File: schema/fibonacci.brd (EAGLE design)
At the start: 88.9 x 59.7 mm, 29 parts, among them IC1 ATMEGA328P, IC2 DS1307

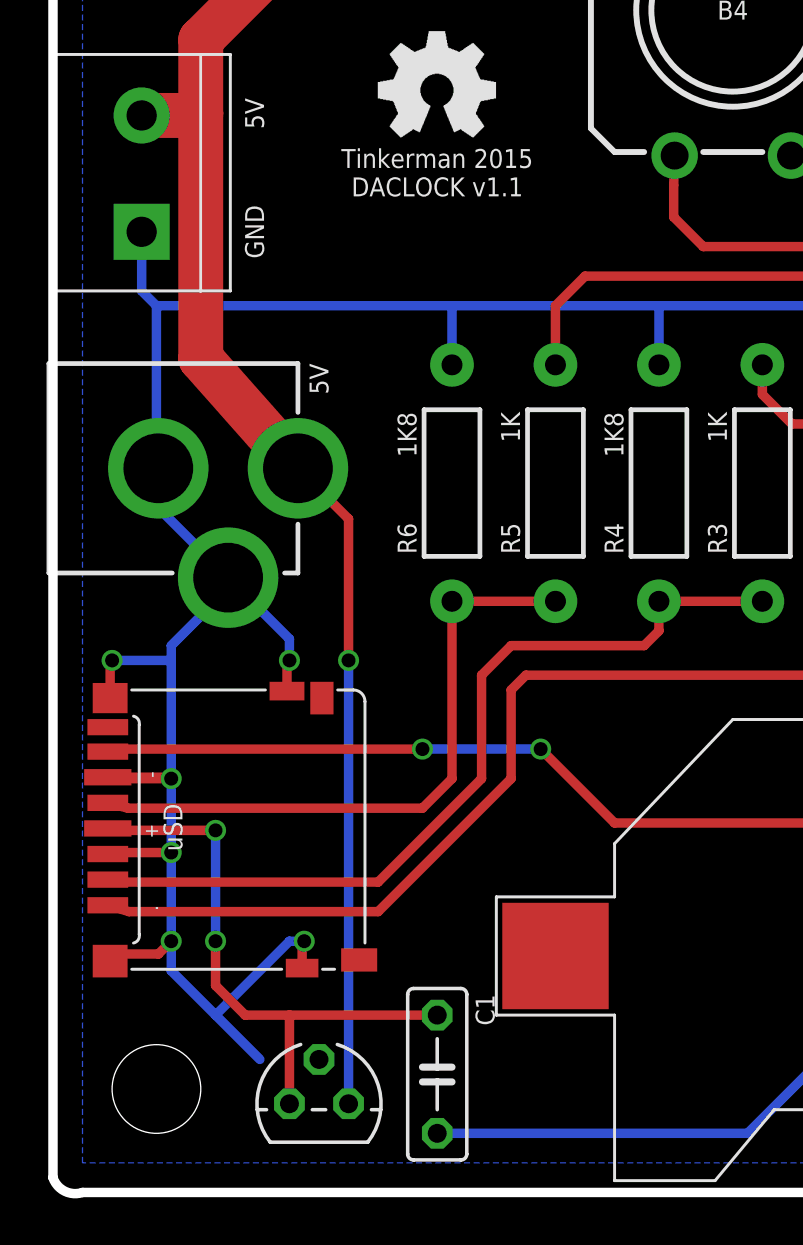
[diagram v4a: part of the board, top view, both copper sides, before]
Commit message: Version 1.2 of the layout sent to fab
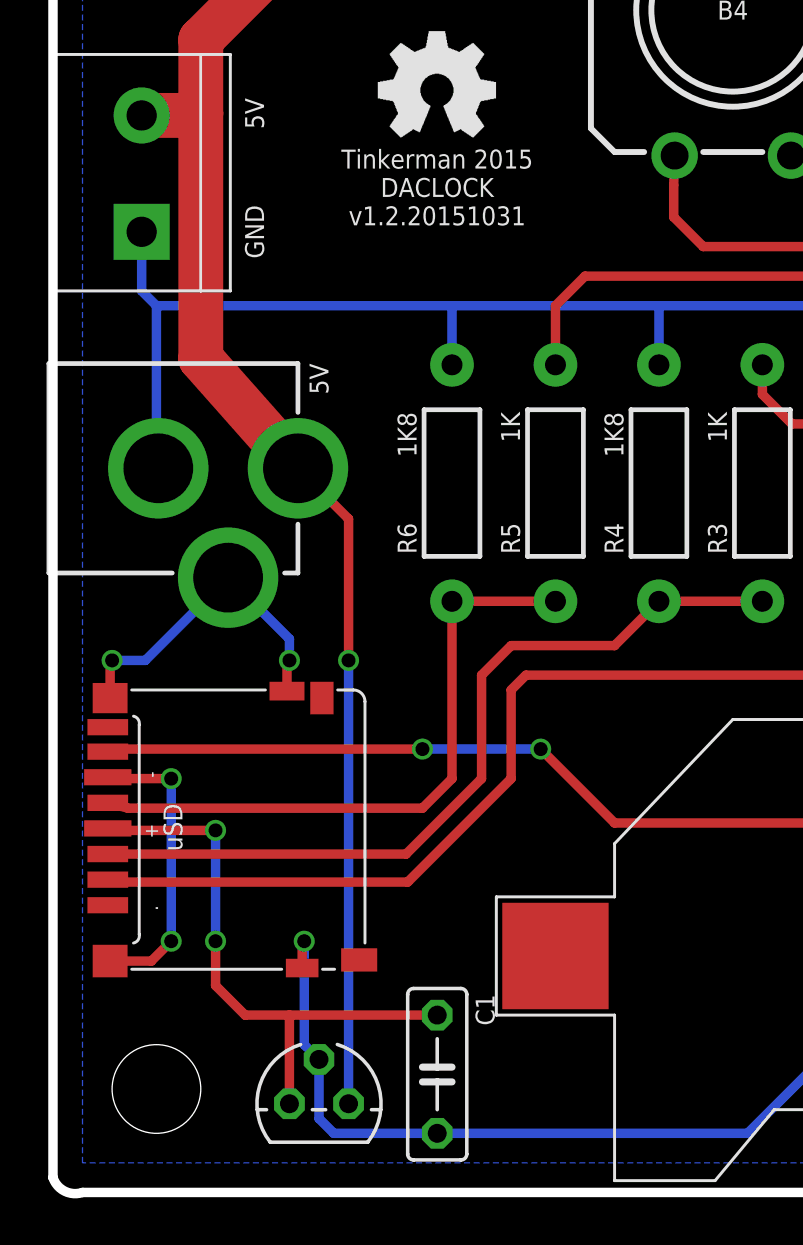
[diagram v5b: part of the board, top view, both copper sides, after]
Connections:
- net GND: no longer U$2.CMD
- net SD_MOSI: now also U$2.CMD; no longer U$2.CD/DAT3
- net SD_SS: now also U$2.CD/DAT3; no longer U$2.DAT2
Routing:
- net GND: track 307.2 -> 290.7 mm, vias 7 -> 6
- net SD_MOSI: track 36.5 -> 35.2 mm
- net SD_SS: track 45.9 -> 45.4 mm
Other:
- board text added: "Tinkerman 2015 DACLOCK v1.2.20151031"
- board text removed: "Tinkerman 2015 DACLOCK v1.1"
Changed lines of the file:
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@@
 <rectangle x1="16.1417" y1="49.8475" x2="16.8529" y2="49.8729" layer="25"/>
 <rectangle x1="16.1417" y1="49.8729" x2="16.8529" y2="49.8983" layer="25"/>
-<text x="16.51" y="43.815" size="0.8128" layer="21" font="vector" ratio="15" align="center">Tinkerman 2015
-DACLOCK v1.1</text>
+<text x="16.51" y="43.18" size="0.8128" layer="21" font="vector" ratio="15" align="center">Tinkerman 2015
+DACLOCK
+v1.2.20151031</text>
 <text x="11.43" y="34.29" size="0.8128" layer="21" font="vector" ratio="15" rot="R90" align="center-left">5V</text>
 </plain>
@@
 <wire x1="85.09" y1="19.685" x2="63.5" y2="19.685" width="0.4064" layer="16"/>
 <wire x1="73.62" y1="55.84" x2="73.66" y2="54.57" width="0.4064" layer="16"/>
-<wire x1="4.525" y1="31.115" x2="4.525" y2="29.415" width="0.4064" layer="16"/>
-<wire x1="4.525" y1="29.415" x2="7.525" y2="26.415" width="0.4064" layer="16"/>
 <wire x1="73.66" y1="54.57" x2="74.93" y2="54.61" width="0.4064" layer="16"/>
 <wire x1="34.925" y1="38.1" x2="26.035" y2="38.1" width="0.4064" layer="16"/>
@@
 <wire x1="66.04" y1="54.61" x2="66.04" y2="40.64" width="0.4064" layer="16"/>
 <wire x1="4.445" y1="38.1" x2="4.445" y2="31.195" width="0.4064" layer="16"/>
-<wire x1="5.08" y1="10.795" x2="5.08" y2="14.605" width="0.4064" layer="16"/>
-<wire x1="7.525" y1="25.94" x2="7.62" y2="26.035" width="0.4064" layer="16"/>
-<wire x1="7.62" y1="26.035" x2="7.62" y2="26.32" width="0.4064" layer="16"/>
-<wire x1="7.62" y1="26.32" x2="7.525" y2="26.415" width="0.4064" layer="16"/>
-<wire x1="7.525" y1="26.415" x2="7.525" y2="25.94" width="0.4064" layer="16"/>
-<wire x1="7.525" y1="25.94" x2="5.08" y2="23.495" width="0.4064" layer="16"/>
-<wire x1="5.08" y1="23.495" x2="5.08" y2="22.86" width="0.4064" layer="16"/>
-<wire x1="5.08" y1="22.86" x2="5.08" y2="17.78" width="0.4064" layer="16"/>
-<wire x1="5.08" y1="17.78" x2="2.415" y2="17.78" width="0.4064" layer="1"/>
-<wire x1="2.415" y1="17.78" x2="2.355" y2="17.84" width="0.4064" layer="1"/>
-<wire x1="2.355" y1="17.84" x2="5.02" y2="17.84" width="0.4064" layer="1"/>
-<wire x1="5.02" y1="17.84" x2="5.08" y2="17.78" width="0.4064" layer="1"/>
-<via x="5.08" y="17.78" extent="1-16" drill="0.6" shape="square"/>
-<wire x1="5.08" y1="17.78" x2="5.08" y2="14.605" width="0.4064" layer="16"/>
-<via x="5.08" y="14.605" extent="1-16" drill="0.6" shape="square"/>
-<wire x1="5.08" y1="9.525" x2="6.985" y2="7.62" width="0.4064" layer="16"/>
-<wire x1="6.985" y1="7.62" x2="8.89" y2="5.715" width="0.4064" layer="16"/>
 <wire x1="16.51" y1="2.54" x2="29.845" y2="2.54" width="0.4064" layer="16"/>
 <wire x1="29.845" y1="2.54" x2="34.29" y2="6.985" width="0.4064" layer="16"/>
@@
 <contactref element="U$2" pad="GND3"/>
 <contactref element="U$2" pad="GND2"/>
-<contactref element="U$2" pad="CMD"/>
-<wire x1="2.455" y1="9.94" x2="2.455" y2="10.245" width="0.4064" layer="1"/>
-<via x="5.08" y="10.795" extent="1-16" drill="0.6" shape="square"/>
-<wire x1="5.08" y1="10.795" x2="5.08" y2="9.525" width="0.4064" layer="16"/>
-<wire x1="10.705" y1="9.64" x2="10.705" y2="10.705" width="0.4064" layer="1"/>
-<wire x1="10.705" y1="10.705" x2="10.795" y2="10.795" width="0.4064" layer="1"/>
-<via x="10.795" y="10.795" extent="1-16" drill="0.6" shape="square"/>
-<wire x1="10.795" y1="10.795" x2="10.16" y2="10.795" width="0.4064" layer="16"/>
-<wire x1="10.16" y1="10.795" x2="6.985" y2="7.62" width="0.4064" layer="16"/>
-<wire x1="10.055" y1="21.54" x2="10.055" y2="22.755" width="0.4064" layer="1"/>
-<wire x1="10.055" y1="22.755" x2="10.16" y2="22.86" width="0.4064" layer="1"/>
-<via x="10.16" y="22.86" extent="1-16" drill="0.6" shape="square"/>
-<wire x1="10.16" y1="22.86" x2="10.16" y2="23.78" width="0.4064" layer="16"/>
-<wire x1="10.16" y1="23.78" x2="7.525" y2="26.415" width="0.4064" layer="16"/>
-<wire x1="2.455" y1="21.24" x2="2.455" y2="22.775" width="0.4064" layer="1"/>
-<wire x1="2.455" y1="22.775" x2="2.54" y2="22.86" width="0.4064" layer="1"/>
-<via x="2.54" y="22.86" extent="1-16" drill="0.6" shape="square"/>
-<wire x1="2.54" y1="22.86" x2="5.08" y2="22.86" width="0.4064" layer="16"/>
-<wire x1="5.08" y1="14.605" x2="2.42" y2="14.605" width="0.4064" layer="1"/>
-<wire x1="2.42" y1="14.605" x2="2.355" y2="14.54" width="0.4064" layer="1"/>
-<wire x1="2.455" y1="10.245" x2="4.53" y2="10.245" width="0.4064" layer="1"/>
-<wire x1="4.53" y1="10.245" x2="5.08" y2="10.795" width="0.4064" layer="1"/>
 <contactref element="POWER_TERMINAL" pad="1"/>
 <wire x1="3.81" y1="41.275" x2="3.81" y2="38.735" width="0.4064" layer="16"/>
@@
 <vertex x="1.27" y="1.27"/>
 </polygon>
+<wire x1="11.43" y1="5.715" x2="11.43" y2="3.175" width="0.4064" layer="16"/>
+<wire x1="11.43" y1="3.175" x2="12.065" y2="2.54" width="0.4064" layer="16"/>
+<wire x1="12.065" y1="2.54" x2="16.51" y2="2.54" width="0.4064" layer="16"/>
+<wire x1="2.455" y1="9.94" x2="4.225" y2="9.94" width="0.4064" layer="1"/>
+<wire x1="4.225" y1="9.94" x2="5.08" y2="10.795" width="0.4064" layer="1"/>
+<via x="5.08" y="10.795" extent="1-16" drill="0.6" shape="square"/>
+<wire x1="5.08" y1="10.795" x2="5.08" y2="17.78" width="0.4064" layer="16"/>
+<via x="5.08" y="17.78" extent="1-16" drill="0.6" shape="square"/>
+<wire x1="5.08" y1="17.78" x2="2.415" y2="17.78" width="0.4064" layer="1"/>
+<wire x1="2.415" y1="17.78" x2="2.355" y2="17.84" width="0.4064" layer="1"/>
+<wire x1="2.455" y1="21.24" x2="2.455" y2="22.775" width="0.4064" layer="1"/>
+<wire x1="2.455" y1="22.775" x2="2.54" y2="22.86" width="0.4064" layer="1"/>
+<via x="2.54" y="22.86" extent="1-16" drill="0.6" shape="square"/>
+<wire x1="2.54" y1="22.86" x2="3.97" y2="22.86" width="0.4064" layer="16"/>
+<wire x1="3.97" y1="22.86" x2="7.525" y2="26.415" width="0.4064" layer="16"/>
+<wire x1="10.055" y1="21.54" x2="10.055" y2="22.755" width="0.4064" layer="1"/>
+<wire x1="10.055" y1="22.755" x2="10.16" y2="22.86" width="0.4064" layer="1"/>
+<via x="10.16" y="22.86" extent="1-16" drill="0.6" shape="square"/>
+<wire x1="10.16" y1="22.86" x2="10.16" y2="23.78" width="0.4064" layer="16"/>
+<wire x1="10.16" y1="23.78" x2="7.525" y2="26.415" width="0.4064" layer="16"/>
+<wire x1="10.705" y1="9.64" x2="10.705" y2="10.705" width="0.4064" layer="1"/>
+<wire x1="10.705" y1="10.705" x2="10.795" y2="10.795" width="0.4064" layer="1"/>
+<via x="10.795" y="10.795" extent="1-16" drill="0.6" shape="square"/>
+<wire x1="10.795" y1="10.795" x2="10.795" y2="6.35" width="0.4064" layer="16"/>
+<wire x1="10.795" y1="6.35" x2="11.43" y2="5.715" width="0.4064" layer="16"/>
 </signal>
 <signal name="5V">
@@
 <contactref element="R1" pad="P$1"/>
 <wire x1="34.925" y1="25.4" x2="39.37" y2="25.4" width="0.4064" layer="1"/>
-<contactref element="U$2" pad="DAT2"/>
+<contactref element="U$2" pad="CD/DAT3"/>
 <wire x1="34.925" y1="25.4" x2="34.925" y2="23.495" width="0.4064" layer="1"/>
 <wire x1="34.925" y1="23.495" x2="33.655" y2="22.225" width="0.4064" layer="1"/>
@@
 <wire x1="20.32" y1="22.225" x2="19.685" y2="21.59" width="0.4064" layer="1"/>
 <wire x1="19.685" y1="21.59" x2="19.685" y2="17.78" width="0.4064" layer="1"/>
-<wire x1="19.685" y1="17.78" x2="13.97" y2="12.065" width="0.4064" layer="1"/>
-<wire x1="13.97" y1="12.065" x2="3.265" y2="12.065" width="0.4064" layer="1"/>
-<wire x1="3.265" y1="12.065" x2="2.355" y2="12.34" width="0.4064" layer="1"/>
+<wire x1="19.685" y1="17.78" x2="15.24" y2="13.335" width="0.4064" layer="1"/>
+<wire x1="15.24" y1="13.335" x2="2.46" y2="13.335" width="0.4064" layer="1"/>
+<wire x1="2.46" y1="13.335" x2="2.355" y2="13.44" width="0.4064" layer="1"/>
 </signal>
 <signal name="SD_MOSI">
@@
 <contactref element="R3" pad="P$1"/>
 <wire x1="26.035" y1="25.4" x2="30.48" y2="25.4" width="0.4064" layer="1"/>
-<contactref element="U$2" pad="CD/DAT3"/>
-<wire x1="26.035" y1="25.4" x2="26.035" y2="24.13" width="0.4064" layer="1"/>
-<wire x1="26.035" y1="24.13" x2="25.4" y2="23.495" width="0.4064" layer="1"/>
-<wire x1="25.4" y1="23.495" x2="19.685" y2="23.495" width="0.4064" layer="1"/>
-<wire x1="19.685" y1="23.495" x2="18.415" y2="22.225" width="0.4064" layer="1"/>
-<wire x1="18.415" y1="22.225" x2="18.415" y2="17.78" width="0.4064" layer="1"/>
-<wire x1="18.415" y1="17.78" x2="13.97" y2="13.335" width="0.4064" layer="1"/>
-<wire x1="13.97" y1="13.335" x2="3.095" y2="13.335" width="0.4064" layer="1"/>
-<wire x1="3.095" y1="13.335" x2="2.355" y2="13.44" width="0.4064" layer="1"/>
+<contactref element="U$2" pad="CMD"/>
+<wire x1="2.355" y1="14.54" x2="15.175" y2="14.54" width="0.4064" layer="1"/>
+<wire x1="15.175" y1="14.54" x2="18.415" y2="17.78" width="0.4064" layer="1"/>
+<wire x1="18.415" y1="17.78" x2="18.415" y2="22.225" width="0.4064" layer="1"/>
+<wire x1="18.415" y1="22.225" x2="19.685" y2="23.495" width="0.4064" layer="1"/>
+<wire x1="19.685" y1="23.495" x2="24.13" y2="23.495" width="0.4064" layer="1"/>
+<wire x1="24.13" y1="23.495" x2="26.035" y2="25.4" width="0.4064" layer="1"/>
 </signal>
 <signal name="SD_SCK">
